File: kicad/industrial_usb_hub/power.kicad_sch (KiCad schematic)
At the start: 0 parts

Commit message: completed schematic
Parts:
- added C38, C42: 22µ, symbol Device:C
- added C39, C43: 6.8n, symbol Device:C
- added C40, C44: 1µ, symbol Device:C
- added C41, C45: 44µ, symbol Device:C
- added L1, L2: 1.5µ, symbol Device:L
- added R15, R19: 20, symbol Device:R
- added R16: 30k, symbol Device:R
- added R17, R21: 40.2k, symbol Device:R
- added R18: 13k, symbol Device:R
- added R20: 75k, symbol Device:R
- added R22: 82k, symbol Device:R
- added R23: 100k, symbol Device:R
- added U8, U9: MP2393GTL-P, SOT583_MP2393, symbol 2026-04-11_17-36-43:MP2393GTL-P
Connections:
- new net: C43.1, U9.7 (SS)
- new net: C44.1, R19.2
- new net: R16.2, R17.1, R18.2
- new net: C39.1, U8.7 (SS)
- new net: R20.2, R21.1, R22.2
- new net: C40.1, R15.2
- new net +1V2: C45.1, L2.2, R21.2
- new net +3V3: C41.1, L1.2, R17.2
- new net BST_1V2: R19.1, U9.5 (BST)
- new net BST_3V3: R15.1, U8.5 (BST)
- new net FB_1V2: R20.1, U9.8 (FB)
- new net FB_3V3: R16.1, U8.8 (FB)
- new net GND: C38.2, C39.2, C41.2, C42.2, C43.2, C45.2, R18.1, R22.1, U8.4 (GND), U9.4 (GND)
- new net PG_3V3: R23.1, U8.1 (PG), U9.6 (EN)
- new net SW_1V2: C44.2, L2.1, U9.3 (SW)
- new net SW_3V3: C40.2, L1.1, U8.3 (SW)
- new net VBUS: C38.1, C42.1, R23.2, U8.2 (IN), U8.6 (EN), U9.2 (IN)
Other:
- title: (none) -> Power

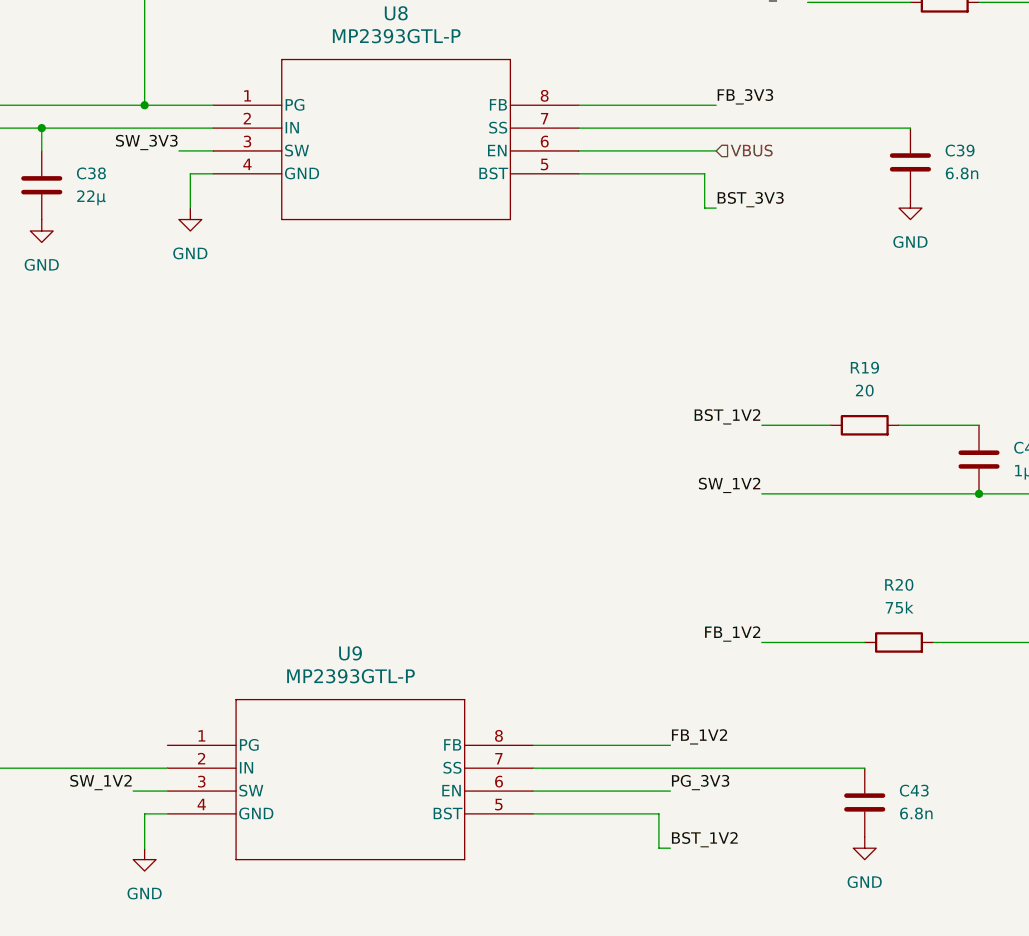
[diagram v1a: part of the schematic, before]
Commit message: assigned footprints
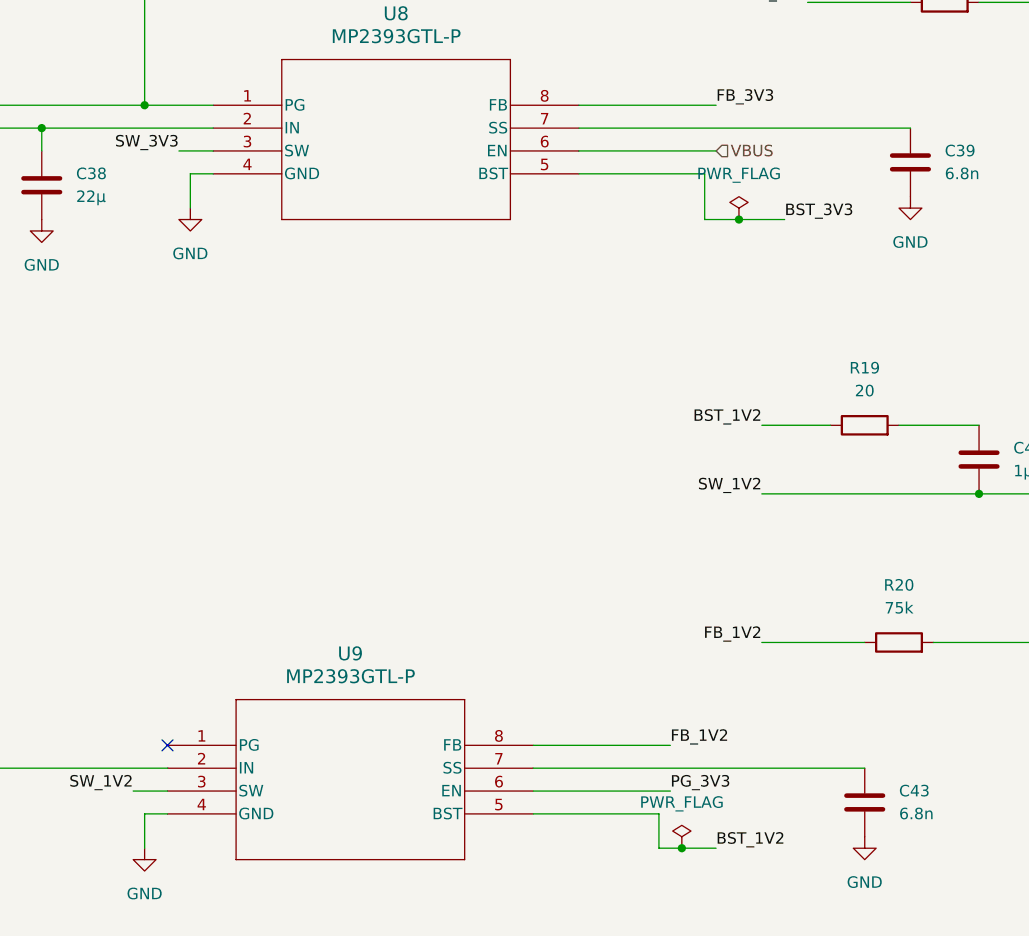
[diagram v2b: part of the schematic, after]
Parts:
- C38, C39, C40, C41, C42, C43, C44, C45: footprint (none) -> Capacitor_SMD:C_0201_0603Metric
- L1, L2: footprint (none) -> Inductor_SMD:L_Taiyo-Yuden_NR-40xx
- R15, R16, R17, R18, R19, R20, R21, R22, R23: footprint (none) -> Resistor_SMD:R_0201_0603Metric
- U8, U9: footprint SOT583_MP2393 -> MP2393GTL-P:SOT583_MP2393
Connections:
- no-connect marks 0 -> 1
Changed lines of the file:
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@@
+	)
+	(junction
+		(at 168.91 80.01)
+		(diameter 0)
+		(color 0 0 0 0)
 	)
 	(junction
@@
 	)
 	(junction
+		(at 162.56 149.86)
+		(diameter 0)
+		(color 0 0 0 0)
+	)
+	(junction
 		(at 252.73 127)
 		(diameter 0)
@@
 		(color 0 0 0 0)
 	)
+	(no_connect
+		(at 105.41 138.43)
+	)
 	(wire
 		(pts
@@
 	(wire
 		(pts
-			(xy 165.1 78.74) (xy 166.37 78.74)
+			(xy 165.1 80.01) (xy 168.91 80.01)
 		)
 		(stroke
@@
 	(wire
 		(pts
-			(xy 160.02 149.86) (xy 161.29 149.86)
+			(xy 168.91 80.01) (xy 173.99 80.01)
+		)
+		(stroke
+			(width 0)
+			(type default)
+		)
+	)
+	(wire
+		(pts
+			(xy 160.02 149.86) (xy 162.56 149.86)
 		)
 		(stroke
@@
 	(wire
 		(pts
-			(xy 165.1 78.74) (xy 165.1 74.93)
+			(xy 165.1 80.01) (xy 165.1 74.93)
 		)
 		(stroke
@@
 	(wire
 		(pts
+			(xy 166.37 149.86) (xy 162.56 149.86)
+		)
+		(stroke
+			(width 0)
+			(type default)
+		)
+	)
+	(wire
+		(pts
 			(xy 243.84 39.37) (xy 257.81 39.37)
 		)
@@
 	)
 	(label "BST_1V2"
-		(at 161.29 149.86 0)
+		(at 166.37 149.86 0)
 		(effects
 			(font
@@
 	)
 	(label "BST_3V3"
-		(at 166.37 78.74 0)
+		(at 173.99 80.01 0)
 		(effects
 			(font
@@
 			)
 		)
-		(property "Footprint" "SOT583_MP2393"
+		(property "Footprint" "MP2393GTL-P:SOT583_MP2393"
 			(at 105.41 138.43 0)
 			(effects
@@
 			)
 		)
-		(property "Footprint" ""
+		(property "Footprint" "Resistor_SMD:R_0201_0603Metric"
 			(at 182.88 104.648 90)
 			(effects
@@
 			)
 		)
-		(property "Footprint" ""
+		(property "Footprint" "Capacitor_SMD:C_0201_0603Metric"
 			(at 183.8452 148.59 0)
 			(effects
@@
 			)
 		)
-		(property "Footprint" ""
+		(property "Footprint" "Resistor_SMD:R_0201_0603Metric"
 			(at 259.588 60.96 90)
 			(effects
@@
 			)
 		)
-		(property "Footprint" ""
+		(property "Footprint" "Resistor_SMD:R_0201_0603Metric"
 			(at 191.77 57.658 90)
 			(effects
@@
 			)
 		)
-		(property "Footprint" ""
+		(property "Footprint" "Resistor_SMD:R_0201_0603Metric"
 			(at 259.588 48.26 90)
 			(effects
@@
 			)
 		)
-		(property "Footprint" ""
+		(property "Footprint" "Capacitor_SMD:C_0201_0603Metric"
 			(at 188.9252 77.47 0)
 			(effects
@@
 			)
 		)
-		(property "Footprint" ""
+		(property "Footprint" "Capacitor_SMD:C_0201_0603Metric"
 			(at 244.8052 46.99 0)
 			(effects
@@
 			)
 		)
-		(property "Footprint" ""
+		(property "Footprint" "Capacitor_SMD:C_0201_0603Metric"
 			(at 239.7252 118.11 0)
 			(effects
@@
 			)
 		)
-		(property "Footprint" ""
+		(property "Footprint" "Resistor_SMD:R_0201_0603Metric"
 			(at 254.508 132.08 90)
 			(effects
@@
 			)
 		)
-		(property "Footprint" ""
+		(property "Footprint" "Inductor_SMD:L_Taiyo-Yuden_NR-40xx"
 			(at 209.55 110.49 0)
 			(effects
@@
 	)
 	(symbol
+		(lib_id "power:PWR_FLAG")
+		(at 162.56 149.86 0)
+		(unit 1)
+		(exclude_from_sim no)
+		(in_bom yes)
+		(on_board yes)
+		(dnp no)
+		(fields_autoplaced yes)
+		(property "Reference" "#FLG06"
+			(at 162.56 147.955 0)
+			(effects
+				(font
+					(size 1.27 1.27)
+				)
+				(hide yes)
+			)
+		)
+		(property "Value" "PWR_FLAG"
+			(at 162.56 144.78 0)
+			(effects
+				(font
+					(size 1.27 1.27)
+				)
+			)
+		)
+		(property "Footprint" ""
+			(at 162.56 149.86 0)
+			(effects
+				(font
+					(size 1.27 1.27)
+				)
+				(hide yes)
+			)
+		)
+		(property "Datasheet" "~"
+			(at 162.56 149.86 0)
+			(effects
+				(font
+					(size 1.27 1.27)
+				)
+				(hide yes)
+			)
+		)
+		(property "Description" "Special symbol for telling ERC where power comes from"
+			(at 162.56 149.86 0)
+			(effects
+				(font
+					(size 1.27 1.27)
+				)
+				(hide yes)
+			)
+		)
+		(pin "1"
+		)
+		(instances
+			(project "industrial_usb_hub"
+				(path "/2bdf928d-3bff-4ef5-bf26-63be25952cbb/0162fdbd-d9d3-4562-8e95-e1eb638f0895"
+					(reference "#FLG06")
+					(unit 1)
+				)
+			)
+		)
+	)
+	(symbol
 		(lib_id "Device:R")
 		(at 252.73 119.38 180)
@@
 			)
 		)
-		(property "Footprint" ""
+		(property "Footprint" "Resistor_SMD:R_0201_0603Metric"
 			(at 254.508 119.38 90)
 			(effects
@@
 			)
 		)
-		(property "Footprint" ""
+		(property "Footprint" "Inductor_SMD:L_Taiyo-Yuden_NR-40xx"
 			(at 214.63 39.37 0)
 			(effects
@@
 			)
 		)
-		(property "Footprint" ""
+		(property "Footprint" "Resistor_SMD:R_0201_0603Metric"
 			(at 186.69 128.778 90)
 			(effects
@@
 			)
 		)
-		(property "Footprint" ""
+		(property "Footprint" "Resistor_SMD:R_0201_0603Metric"
 			(at 104.648 50.8 90)
 			(effects
@@
 			)
 		)
-		(property "Footprint" ""
+		(property "Footprint" "Capacitor_SMD:C_0201_0603Metric"
 			(at 201.6252 39.37 0)
 			(effects
@@
 			)
 		)
-		(property "Footprint" ""
+		(property "Footprint" "Capacitor_SMD:C_0201_0603Metric"
 			(at 79.7052 151.13 0)
 			(effects
@@
 	)
 	(symbol
+		(lib_id "power:PWR_FLAG")
+		(at 168.91 80.01 0)
+		(unit 1)
+		(exclude_from_sim no)
+		(in_bom yes)
+		(on_board yes)
+		(dnp no)
+		(fields_autoplaced yes)
+		(property "Reference" "#FLG07"
+			(at 168.91 78.105 0)
+			(effects
+				(font
+					(size 1.27 1.27)
+				)
+				(hide yes)
+			)
+		)
+		(property "Value" "PWR_FLAG"
+			(at 168.91 74.93 0)
+			(effects
+				(font
+					(size 1.27 1.27)
+				)
+			)
+		)
+		(property "Footprint" ""
+			(at 168.91 80.01 0)
+			(effects
+				(font
+					(size 1.27 1.27)
+				)
+				(hide yes)
+			)
+		)
+		(property "Datasheet" "~"
+			(at 168.91 80.01 0)
+			(effects
+				(font
+					(size 1.27 1.27)
+				)
+				(hide yes)
+			)
+		)
+		(property "Description" "Special symbol for telling ERC where power comes from"
+			(at 168.91 80.01 0)
+			(effects
+				(font
+					(size 1.27 1.27)
+				)
+				(hide yes)
+			)
+		)
+		(pin "1"
+		)
+		(instances
+			(project "industrial_usb_hub"
+				(path "/2bdf928d-3bff-4ef5-bf26-63be25952cbb/0162fdbd-d9d3-4562-8e95-e1eb638f0895"
+					(reference "#FLG07")
+					(unit 1)
+				)
+			)
+		)
+	)
+	(symbol
 		(lib_id "power:GND")
 		(at 257.81 71.12 0)
@@
 			)
 		)
-		(property "Footprint" ""
+		(property "Footprint" "Capacitor_SMD:C_0201_0603Metric"
 			(at 92.4052 80.01 0)
 			(effects
@@
 			)
 		)
-		(property "Footprint" ""
+		(property "Footprint" "Resistor_SMD:R_0201_0603Metric"
 			(at 187.96 33.528 90)
 			(effects
@@
 			)
 		)
-		(property "Footprint" "SOT583_MP2393"
+		(property "Footprint" "MP2393GTL-P:SOT583_MP2393"
 			(at 110.49 67.31 0)
 			(effects
@@
 			)
 		)
-		(property "Footprint" ""
+		(property "Footprint" "Capacitor_SMD:C_0201_0603Metric"
 			(at 196.5452 110.49 0)
 			(effects

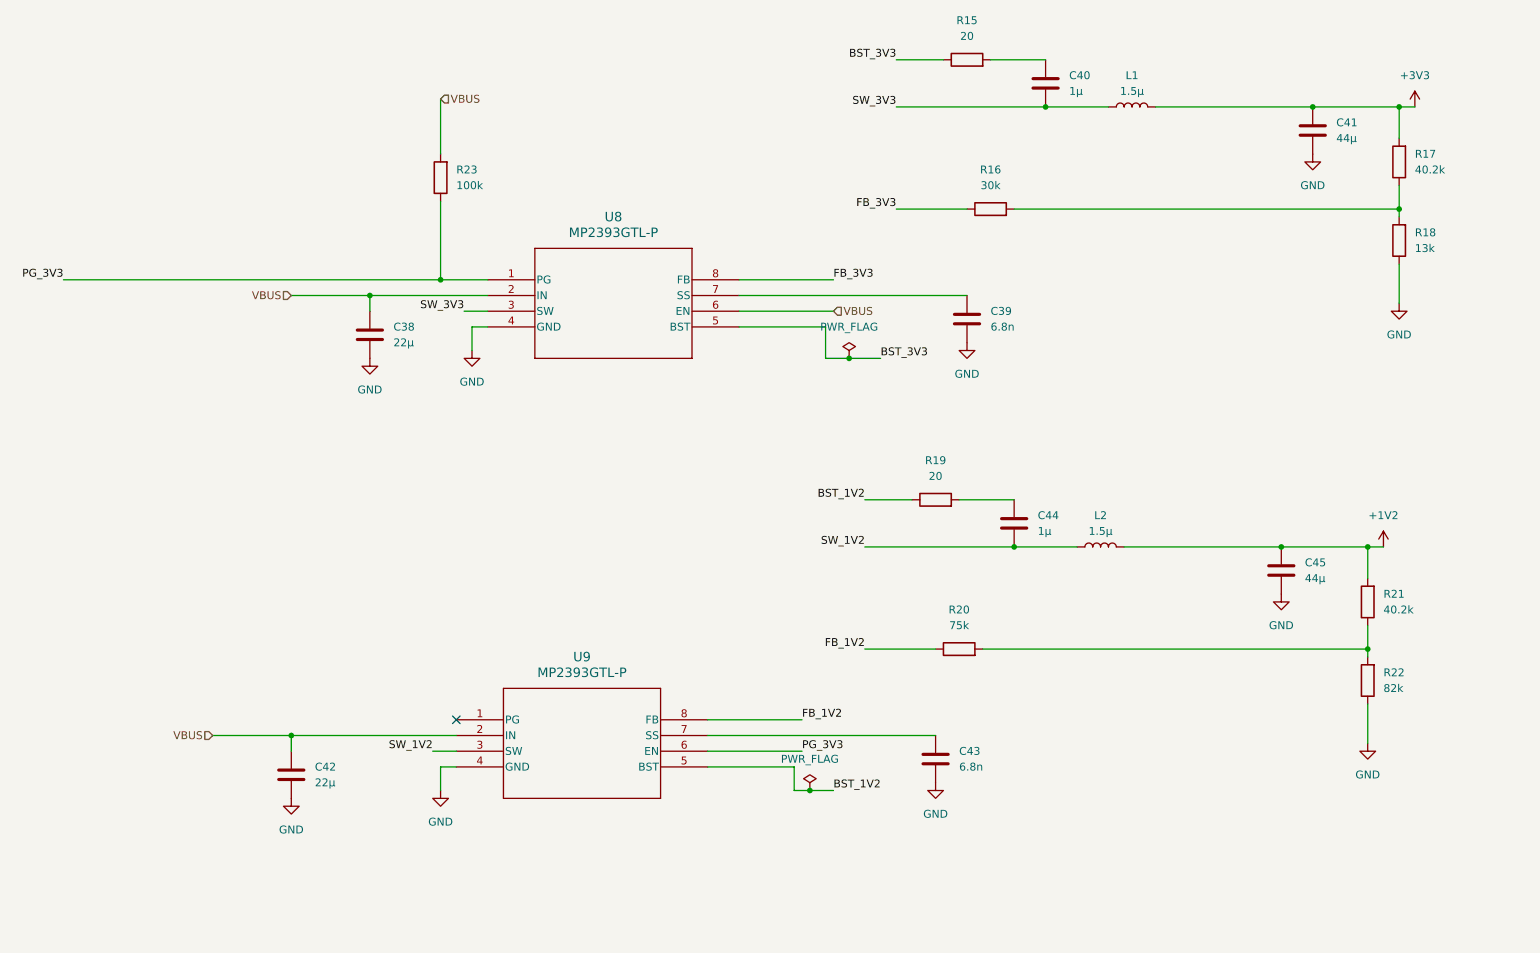
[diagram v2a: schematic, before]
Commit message: added testpoints
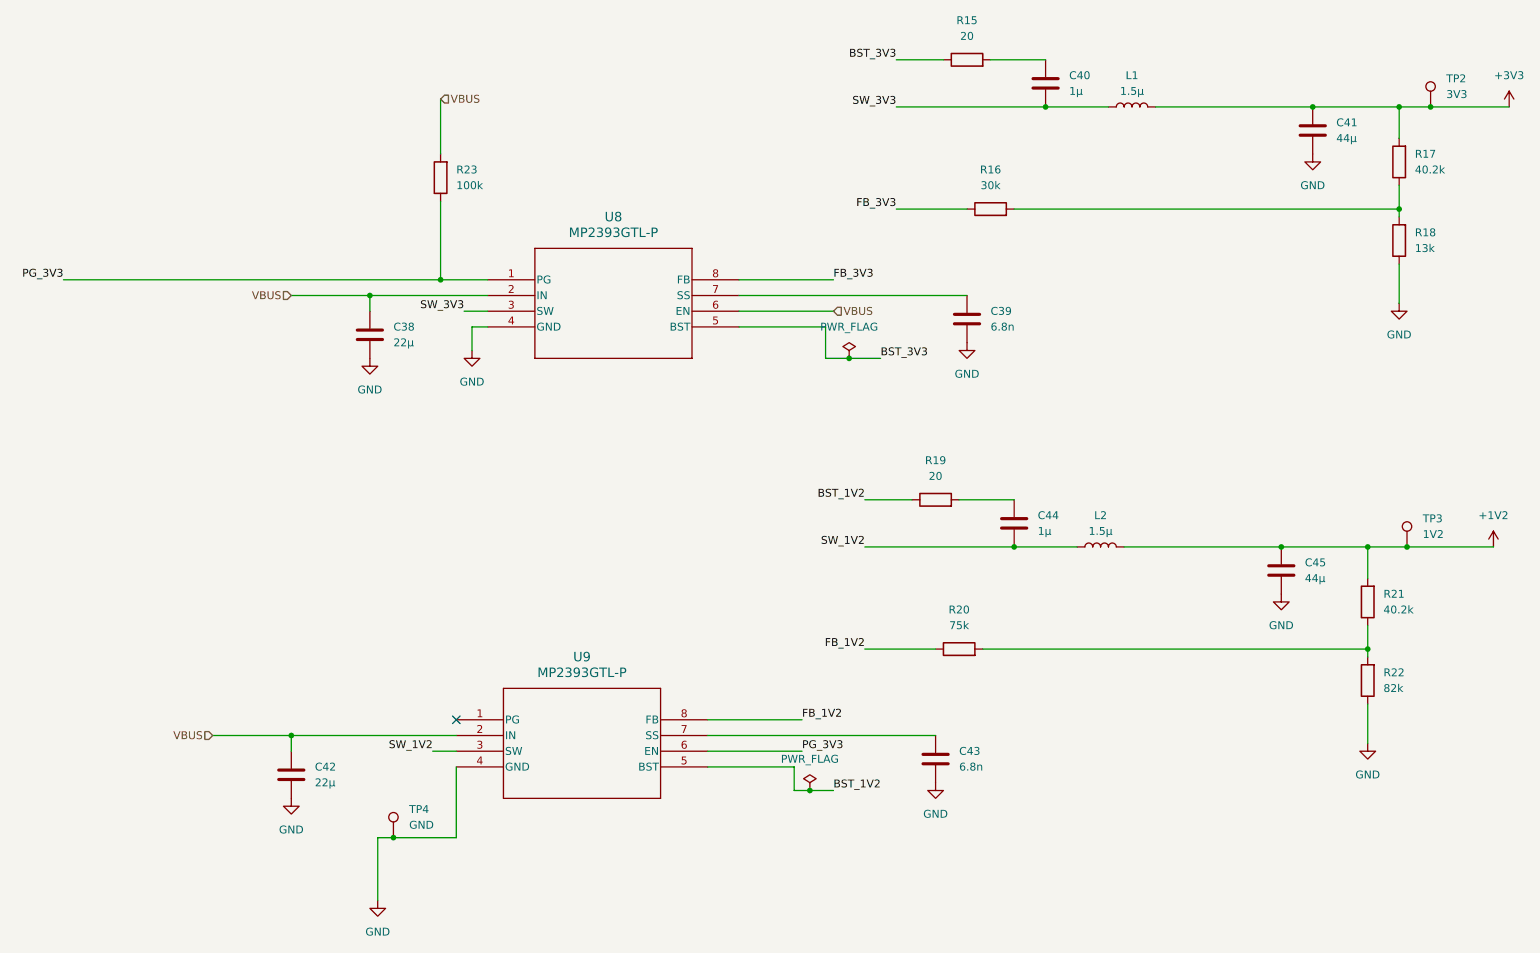
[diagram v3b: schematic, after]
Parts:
- added TP2: 3V3, TestPoint:TestPoint_Pad_1.0x1.0mm, symbol Connector:TestPoint
- added TP3: 1V2, TestPoint:TestPoint_Pad_1.0x1.0mm, symbol Connector:TestPoint
- added TP4: GND, TestPoint:TestPoint_Pad_1.0x1.0mm, symbol Connector:TestPoint
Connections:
- net +1V2: now also TP3.1
- net +3V3: now also TP2.1
- net GND: now also TP4.1
